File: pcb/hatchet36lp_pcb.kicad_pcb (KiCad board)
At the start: 2 copper layers, 180 x 82 mm, 81 parts, among them J1 Conn_01x02_Female, J2 Conn_01x02_Female, J3 Conn_01x04_Female, SW1 SW_Push, SW10 SW_Push, SW11 SW_Push, SW12 SW_Push, SW13 SW_Push, SW14 SW_Push, SW15 SW_Push, SW16 SW_Push, SW17 SW_Push, SW18 SW_Push, SW19 SW_Push, SW2 SW_Push, SW20 SW_Push, SW21 SW_Push, SW22 SW_Push, SW23 SW_Push, SW24 SW_Push, SW25 SW_Push, SW26 SW_Push, SW27 SW_Push, SW28 SW_Push, SW29 SW_Push, SW3 SW_Push, SW30 SW_Push, SW31 SW_Push, SW32 SW_Push, SW33 SW_Push, SW34 SW_Push, SW35 SW_Push, SW36 SW_Push, SW37 SW_Push, SW38 SW_SPDT, SW4 SW_Push, SW5 SW_Push, SW6 SW_Push, SW7 SW_Push, SW8 SW_Push, SW9 SW_Push, U1 BL652

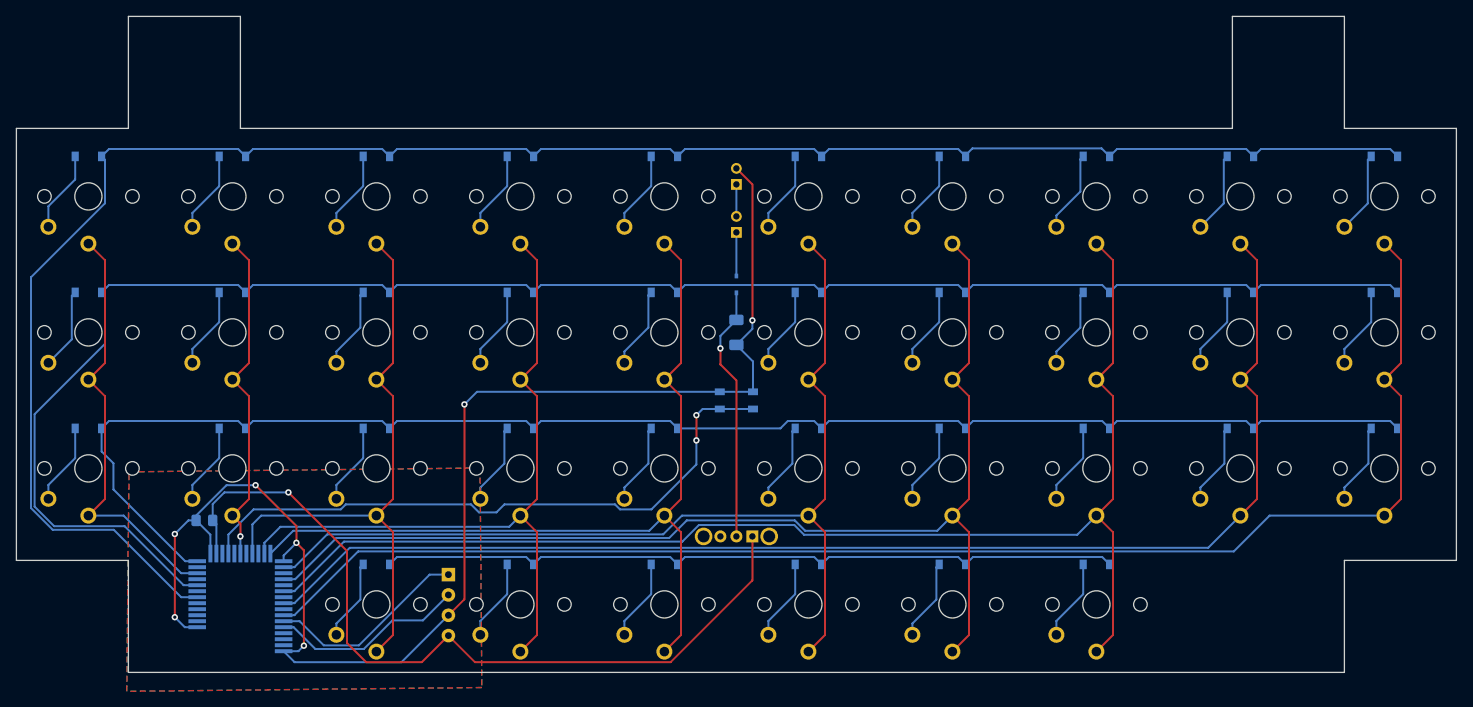
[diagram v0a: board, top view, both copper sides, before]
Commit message: shrink pcb 0.2mm to secure clearance
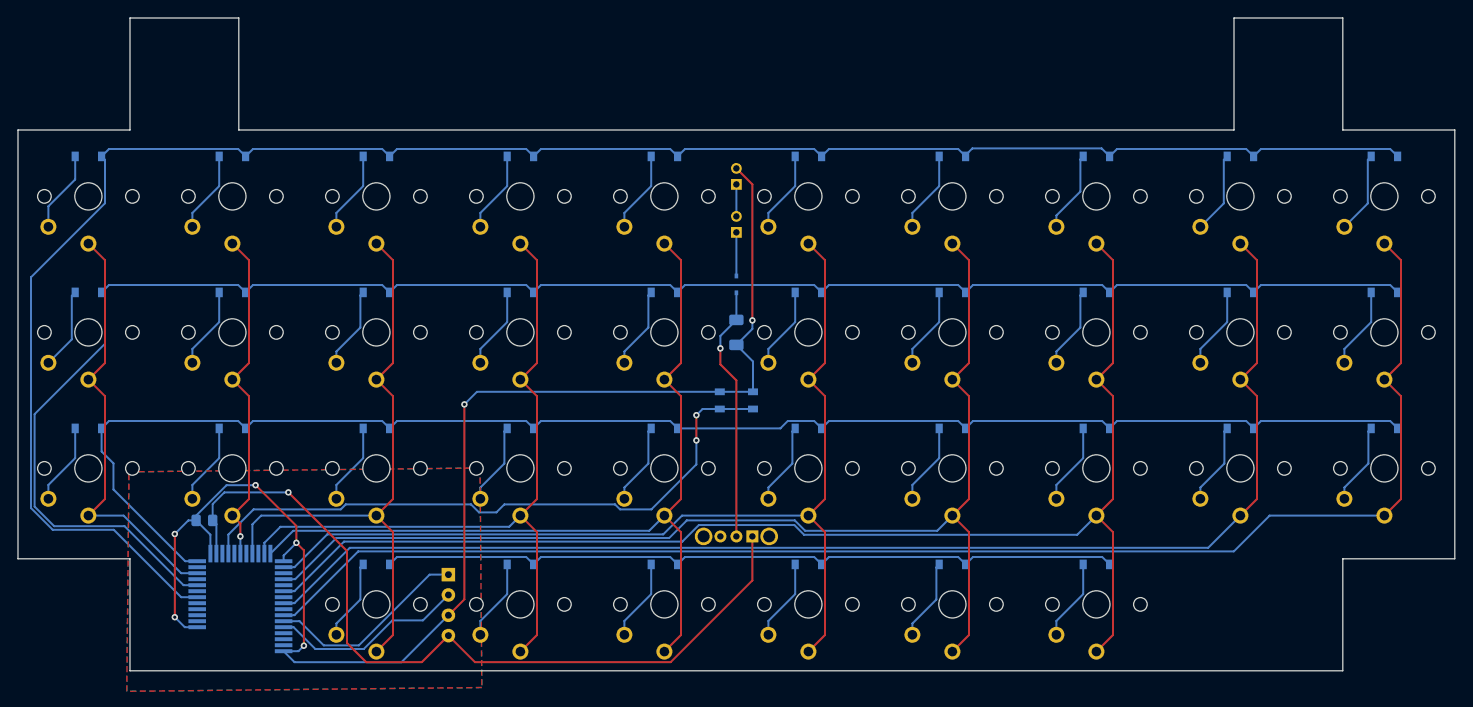
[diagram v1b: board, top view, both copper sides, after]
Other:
- board size 180 x 82 mm -> 179.6 x 81.6 mm
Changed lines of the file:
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@@
     (fp_line (start 0.25 0) (end 0.75 0) (layer "B.Fab") (width 0.1))
     (fp_line (start -0.35 0) (end -0.35 0.55) (layer "B.Fab") (width 0.1))
-    (fp_line (start -0.75 0) (end -0.35 0) (layer "B.Fab") (width 0.1))
-    (fp_line (start 1.4 -0.9) (end -1.4 -0.9) (layer "B.Fab") (width 0.1))
+    (fp_line (start 1.4 -0.9) (end -1.4 -0.9) (layer "B.Fab") (width 0.1))
+    (fp_line (start -0.75 0) (end -0.35 0) (layer "B.Fab") (width 0.1))
     (fp_line (start -0.35 0) (end 0.25 0.4) (layer "B.Fab") (width 0.1))
     (fp_line (start -0.35 0) (end -0.35 -0.55) (layer "B.Fab") (width 0.1))
@@
     )
   )
-  (gr_line (start 202 50) (end 202 36) (layer "Edge.Cuts") (width 0.1))
-  (gr_line (start 64 118) (end 216 118) (layer "Edge.Cuts") (width 0.1))
-  (gr_line (start 216 50) (end 230 50) (layer "Edge.Cuts") (width 0.1))
-  (gr_line (start 216 118) (end 216 104) (layer "Edge.Cuts") (width 0.1))
-  (gr_line (start 216 36) (end 216 50) (layer "Edge.Cuts") (width 0.1))
-  (gr_line (start 202 36) (end 216 36) (layer "Edge.Cuts") (width 0.1))
-  (gr_line (start 64 104) (end 64 118) (layer "Edge.Cuts") (width 0.1))
-  (gr_line (start 78 36) (end 78 50) (layer "Edge.Cuts") (width 0.1))
-  (gr_line (start 64 50) (end 64 36) (layer "Edge.Cuts") (width 0.1))
-  (gr_line (start 78 50) (end 202 50) (layer "Edge.Cuts") (width 0.1))
-  (gr_line (start 50 104) (end 64 104) (layer "Edge.Cuts") (width 0.1))
-  (gr_line (start 50 50) (end 64 50) (layer "Edge.Cuts") (width 0.1))
-  (gr_line (start 230 104) (end 230 50) (layer "Edge.Cuts") (width 0.1))
-  (gr_line (start 216 104) (end 230 104) (layer "Edge.Cuts") (width 0.1))
-  (gr_line (start 64 36) (end 78 36) (layer "Edge.Cuts") (width 0.1))
-  (gr_line (start 50 50) (end 50 104) (layer "Edge.Cuts") (width 0.1))
+  (gr_line (start 202.2 50.2) (end 202.2 36.2) (layer "Edge.Cuts") (width 0.1))
+  (gr_line (start 64.2 117.8) (end 215.8 117.8) (layer "Edge.Cuts") (width 0.1))
+  (gr_line (start 215.8 50.2) (end 229.8 50.2) (layer "Edge.Cuts") (width 0.1))
+  (gr_line (start 215.8 117.8) (end 215.8 103.8) (layer "Edge.Cuts") (width 0.1))
+  (gr_line (start 215.8 36.2) (end 215.8 50.2) (layer "Edge.Cuts") (width 0.1))
+  (gr_line (start 202.2 36.2) (end 215.8 36.2) (layer "Edge.Cuts") (width 0.1))
+  (gr_line (start 64.2 103.8) (end 64.2 117.8) (layer "Edge.Cuts") (width 0.1))
+  (gr_line (start 77.8 36.2) (end 77.8 50.2) (layer "Edge.Cuts") (width 0.1))
+  (gr_line (start 64.2 50.2) (end 64.2 36.2) (layer "Edge.Cuts") (width 0.1))
+  (gr_line (start 77.8 50.2) (end 202.2 50.2) (layer "Edge.Cuts") (width 0.1))
+  (gr_line (start 50.2 103.8) (end 64.2 103.8) (layer "Edge.Cuts") (width 0.1))
+  (gr_line (start 50.2 50.2) (end 64.2 50.2) (layer "Edge.Cuts") (width 0.1))
+  (gr_line (start 229.8 103.8) (end 229.8 50.2) (layer "Edge.Cuts") (width 0.1))
+  (gr_line (start 215.8 103.8) (end 229.8 103.8) (layer "Edge.Cuts") (width 0.1))
+  (gr_line (start 64.2 36.2) (end 77.8 36.2) (layer "Edge.Cuts") (width 0.1))
+  (gr_line (start 50.2 50.2) (end 50.2 103.8) (layer "Edge.Cuts") (width 0.1))
   (gr_text "VDD" (at 136.7 56.9) (layer "B.SilkS")
     (effects (font (size 1 1) (thickness 0.15)) (justify mirror))

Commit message: mod silk for jlcpcb order
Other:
- board text added: "JLCJLCJLCJLC"
- board text added: "hatchet36lp v1"
- board text removed: "hatchet36lp v1 by ak1_"
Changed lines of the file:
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@@
     (effects (font (size 1 1) (thickness 0.15)) (justify mirror))
   )
-  (gr_text "hatchet36lp v1 by ak1_" (at 205.1 115.4) (layer "B.SilkS")
+  (gr_text "hatchet36lp v1" (at 204.7 113.9) (layer "B.SilkS")
     (effects (font (size 1 1) (thickness 0.15)) (justify mirror))
   )
@@
     (effects (font (size 1 1) (thickness 0.15)) (justify mirror))
   )
+  (gr_text "JLCJLCJLCJLC" (at 71.1 43.2) (layer "B.SilkS")
+    (effects (font (size 1 1) (thickness 0.2)) (justify mirror))
+  )
   (gr_text "GND" (at 136.8 60.9) (layer "B.SilkS")
